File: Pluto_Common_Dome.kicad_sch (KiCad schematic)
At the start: 36 parts

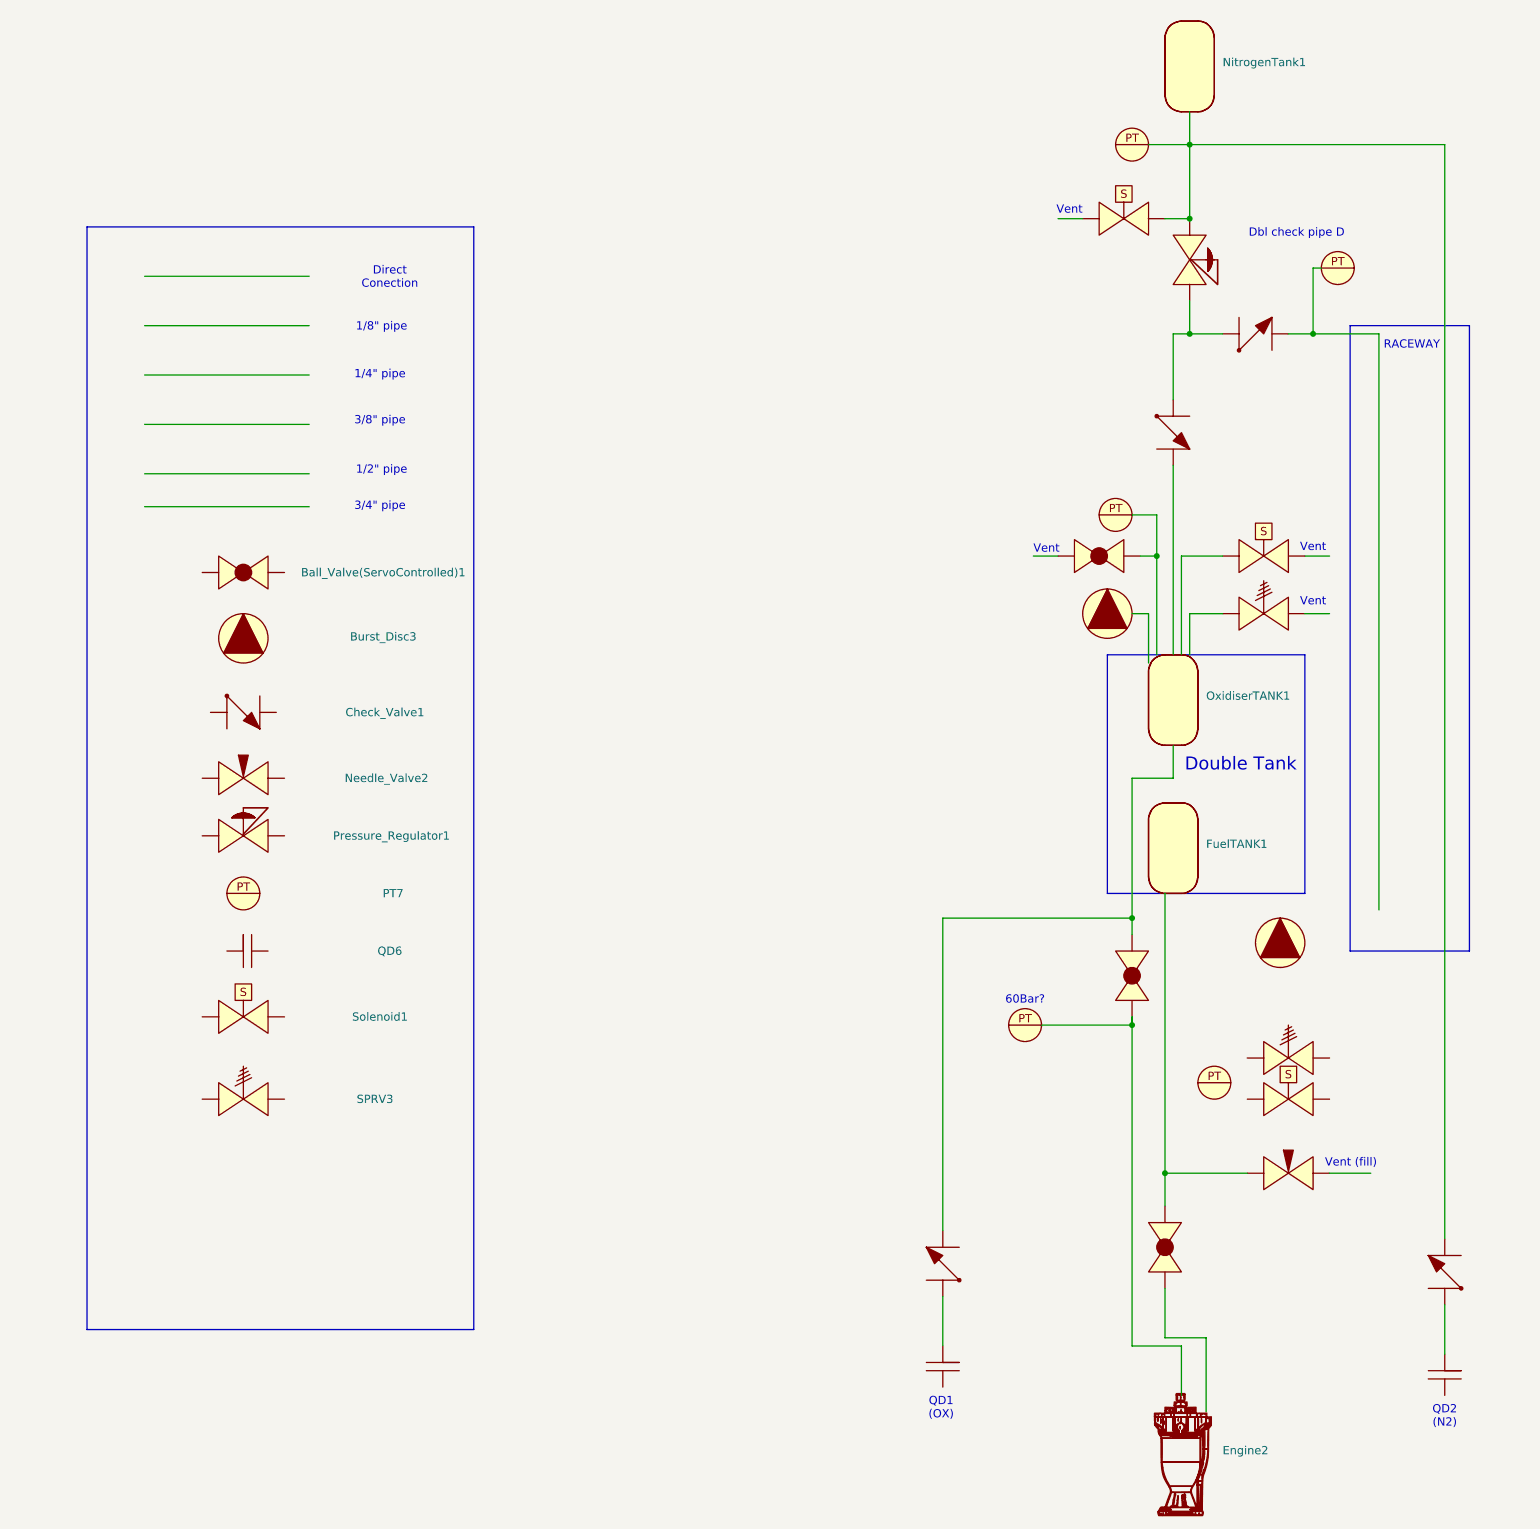
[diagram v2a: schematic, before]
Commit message: Updated Pluto P&ID
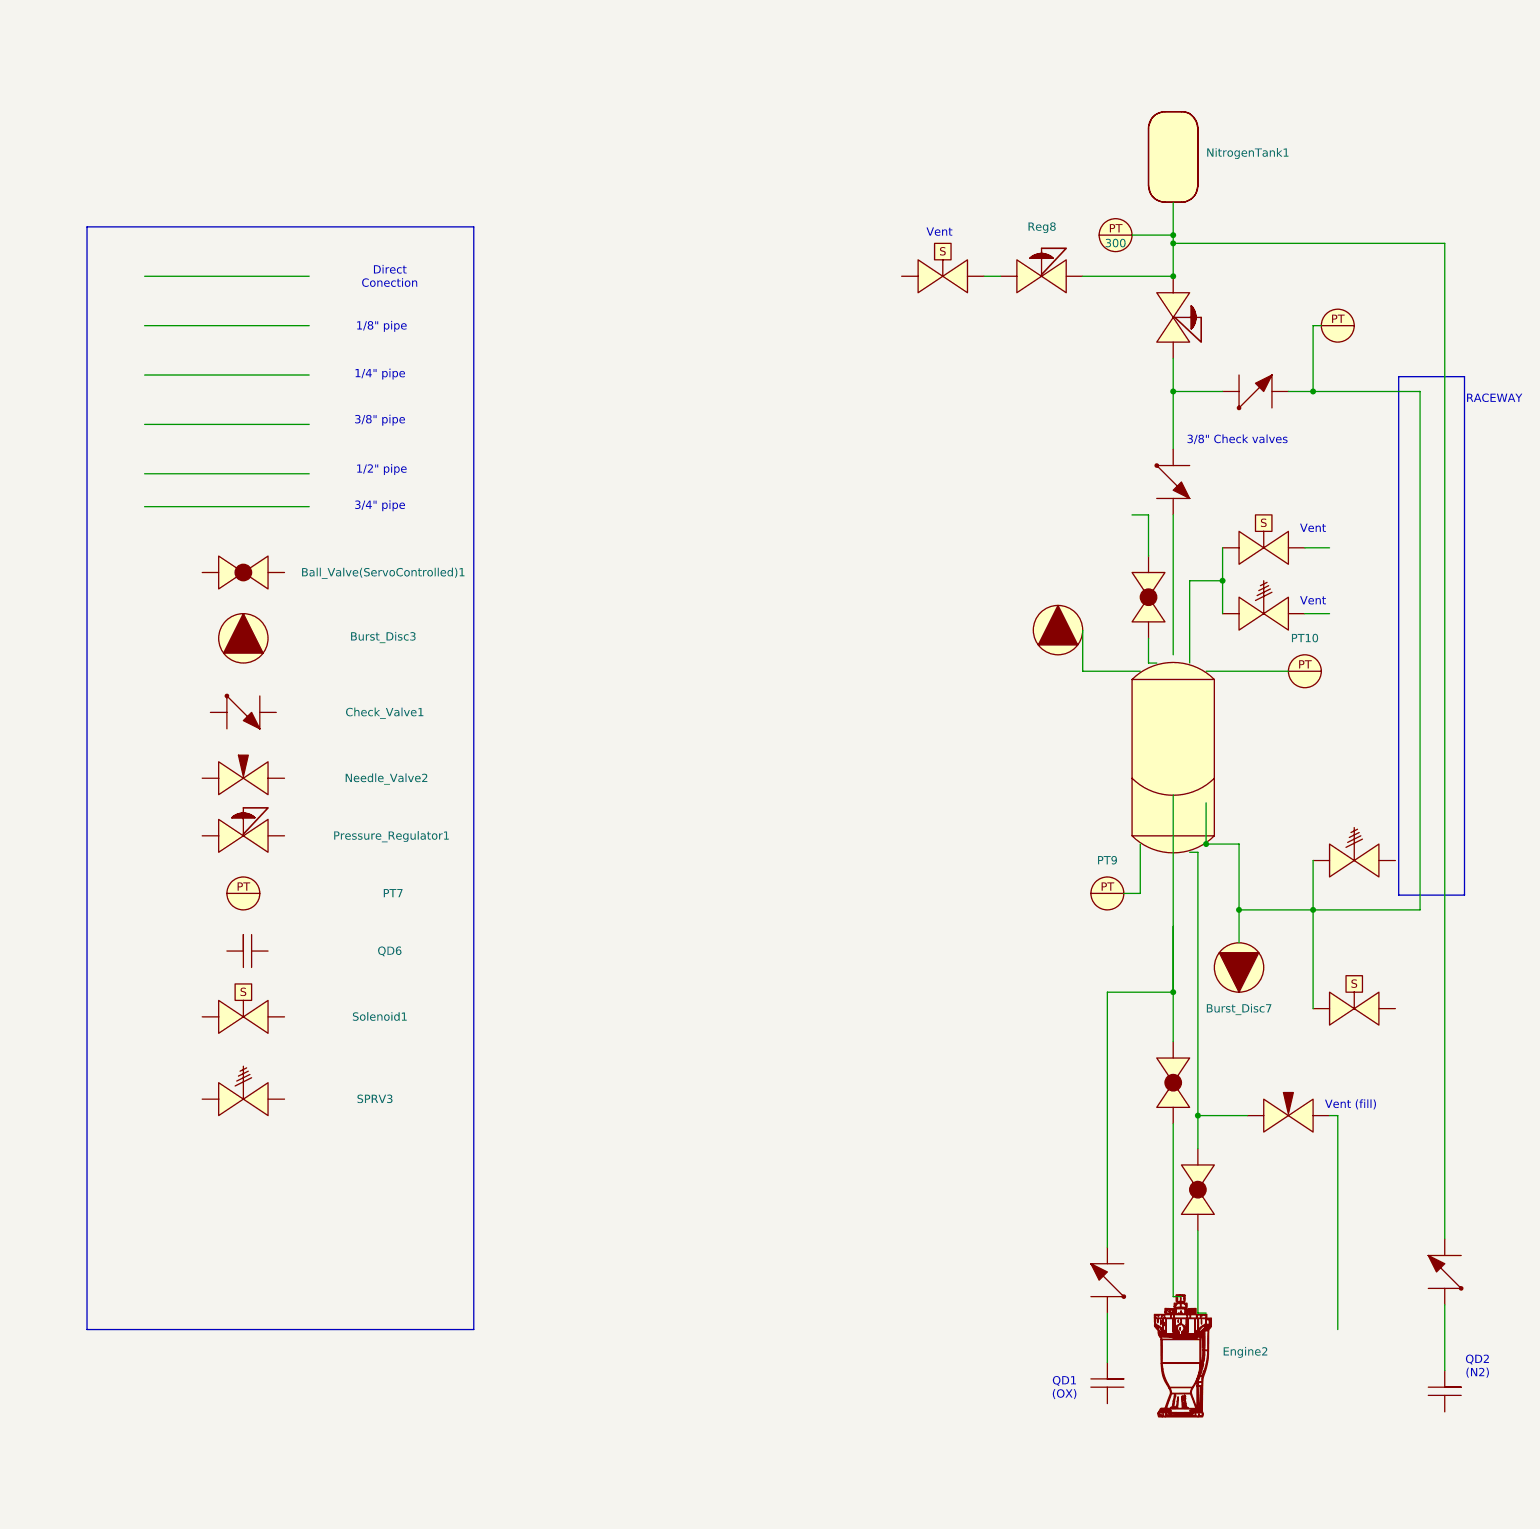
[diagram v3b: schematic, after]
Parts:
- removed Burst_Disc5: ~, symbol PID_symbols:Burst_Disc
- removed FuelTANK1, OxidiserTANK1: ~, symbol PID_symbols:Tank
- removed PT13: ~, symbol PID_symbols:Pressure_Transducer
- added Burst_Disc7: ~, symbol PID_symbols:Burst_Disc
- added CommonDomeTank1: ~, symbol PID_symbols:Common_Dome_Tank
- added Reg8: ~, symbol PID_symbols:Pressure_Regulator
- PT11: value ~ -> 300
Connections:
- net at Solenoid4.: now also Check_Valve4., PT14., SPRV5., Burst_Disc7., CommonDomeTank1.
- net at PT9.: now also CommonDomeTank1.
- net at Solenoid3.: now also SPRV4., CommonDomeTank1.
- net at Ball_Valve2.: now also Engine2.; no longer Check_Valve2.
- net at Needle_Valve3.: no longer Ball_Valve3.
- net at Check_Valve2.: now also QD8.; no longer QD7.
- net at Ball_Valve1.: now also CommonDomeTank1.
- net at PT10.: now also CommonDomeTank1.; no longer Ball_Valve1.
- net at Check_Valve5.: now also QD7.; no longer QD8.
- net at Burst_Disc4.: now also CommonDomeTank1.
- new net: Ball_Valve2., Check_Valve2., CommonDomeTank1.
- new net: Ball_Valve3., CommonDomeTank1., Needle_Valve3.
- new net: Check_Valve5., NitrogenTank1., PT11., Pressure_Regulator2., Reg8.
- new net: Reg8., Solenoid2.
- now unconnected: Engine2., NitrogenTank1., PT11., PT14., Solenoid2.
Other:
- note added: "3/8" Check valves"
- note removed: "60Bar?"
- note removed: "Dbl check pipe D"
- note removed: "Double Tank"
- moved on the sheet: Engine2, NitrogenTank1

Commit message: added universal key
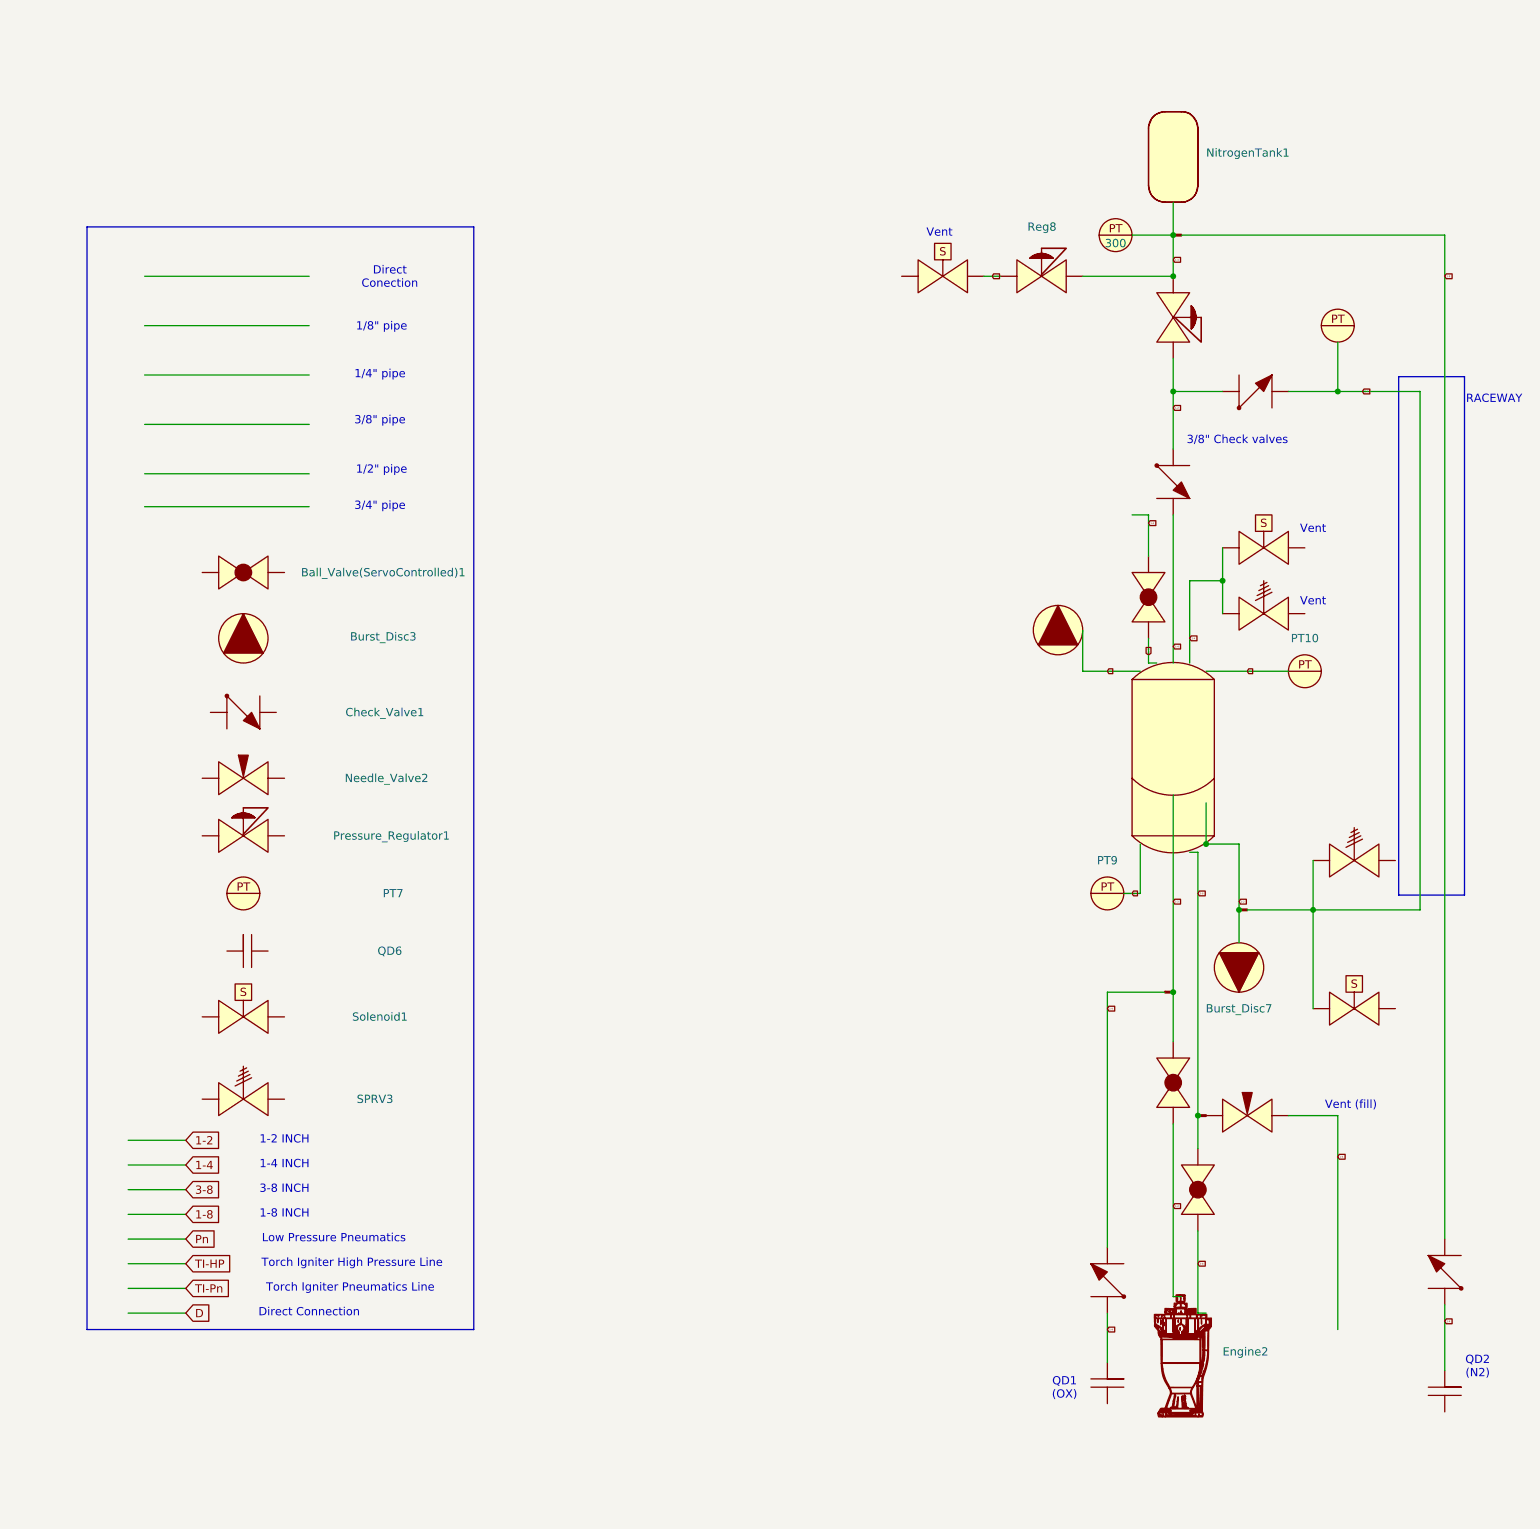
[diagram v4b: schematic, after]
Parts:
- added U2, U3, U4, U5: ~, symbol PID_symbols:stop
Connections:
- net 1-4: now reaches Solenoid4.
- net 1-4: now also Ball_Valve1., Check_Valve2., Check_Valve3., Check_Valve4., Check_Valve5., CommonDomeTank1., Needle_Valve3., NitrogenTank1., PT11., PT14., Pressure_Regulator2., QD7., QD8., Reg8., SPRV4., SPRV5., Solenoid2., Solenoid3., U2., U3., U5.
- net D: now reaches PT10.
- net D: now also Burst_Disc4., CommonDomeTank1., PT9.
- net 1-2: now reaches Ball_Valve2., Engine2.
- net 1-2: now also Burst_Disc7., Check_Valve3., Check_Valve4., CommonDomeTank1., Pressure_Regulator2., U2., U3.
- net 3-8: now reaches Ball_Valve3., Engine2.
- net 3-8: now also CommonDomeTank1., U4.
- net 1-8: now reaches Check_Valve5.
- net 1-8: now also U5.; no longer QD7.
- new net: Needle_Valve3., U4.
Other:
- note added: "1-2 INCH"
- note added: "1-4 INCH"
- note added: "1-8 INCH"
- note added: "3-8 INCH"
- note added: "Direct Connection"
- note added: "Low Pressure Pneumatics"
- note added: "Torch Igniter High Pressure Line"
- note added: "Torch Igniter Pneumatics Line"

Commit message: Small visual changes
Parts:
- added CommonDomeTank2: ~, symbol PID_symbols:Common_Dome_Tank
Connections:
- new net: Needle_Valve3., U4.
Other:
- note added: "Common Dome Tank (Oxidiser upper section, fuel lower section)"
- note added: "Pressure Transducer"
- note added: "Quick Disconnect"
- note added: "Safety Pressure Relief Valve"
- note removed: "1/2" pipe"
- note removed: "1/4" pipe"
- note removed: "1/8" pipe"
- note removed: "3/4" pipe"
- note removed: "3/8" pipe"
- note removed: "Direct Conection"
- moved on the sheet: Ball_Valve(ServoControlled)1, Burst_Disc3, Check_Valve1, Needle_Valve2, Pressure_Regulator1, Solenoid1

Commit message: Pluto pts
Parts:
- added PT15, PT37, PT38: ~, symbol PID_symbols:Pressure_Transducer
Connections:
- net 1-2: now also PT38.
- net 3-8: now also PT15.
- new net: Needle_Valve3., U4.
- new net: Engine2., PT37.

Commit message: sensibl4
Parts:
- added Engine3: ~, symbol PID_symbols:Engine
- added Tank200: Pressurant Tank, symbol PID_symbols:Tank
- Ball_Valve(ServoControlled)100: renamed from Ball_Valve(ServoControlled)1; value ~ -> Servo Controlled Ball Valve
- BurstDisc123: renamed from Burst_Disc3; value ~ -> Burst Disc
- Check_Valve112: renamed from Check_Valve1; value ~ -> Check Valve
- Pressure_Regulator123: renamed from Pressure_Regulator1; value ~ -> Pressure Regulator
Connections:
- net at PT37.: no longer Engine2.
- new net: Needle_Valve3., U4.
- new net: Engine2., PT37.
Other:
- note added: "Engine"
- note added: "Fuel Fill"
- note added: "Manual Valve"
- note added: "Solenoid Valve"
- note removed: "3/8" Check valves"
- note removed: "Vent"
- note removed: "Vent (fill)"
- title: Pluto Common Dome P&ID -> Pluto Propulsion P&ID

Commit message: ereg
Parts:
- removed Pressure_Regulator2: ~, symbol PID_symbols:Pressure_Regulator
- added BV11: ~, symbol PID_symbols:Ball_Valve
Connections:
- net 1-2: no longer Check_Valve3., Check_Valve4.
- net 1-4: now also BV11.
- net 3-8: now also Check_Valve3., Check_Valve4., BV11.
- net at PT37.: no longer Engine2.
- new net: Needle_Valve3., U4.
- new net: Engine2., PT37.
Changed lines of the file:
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@@
+	)
+	(junction
+		(at 144.78 55.88)
+		(diameter 0)
+		(color 0 0 0 0)
 	)
 	(junction
@@
 	)
 	(junction
-		(at 144.78 55.88)
-		(diameter 0)
-		(color 0 0 0 0)
-	)
-	(junction
 		(at 148.59 185.42)
 		(diameter 0)
@@
 	(wire
 		(pts
-			(xy 144.78 68.58) (xy 144.78 73.66)
-		)
-		(stroke
-			(width 0)
-			(type default)
-		)
-	)
-	(wire
-		(pts
 			(xy 140.97 115.57) (xy 142.24 115.57)
 		)
@@
 		(pts
 			(xy 138.43 92.71) (xy 140.97 92.71)
+		)
+		(stroke
+			(width 0)
+			(type default)
+		)
+	)
+	(wire
+		(pts
+			(xy 144.78 72.39) (xy 144.78 73.66)
 		)
 		(stroke
@@
 	(wire
 		(pts
+			(xy 144.78 59.69) (xy 144.78 55.88)
+		)
+		(stroke
+			(width 0)
+			(type default)
+		)
+	)
+	(wire
+		(pts
 			(xy 152.4 102.87) (xy 152.4 107.95)
 		)
@@
 		)
 	)
-	(global_label "1-2"
+	(global_label "3-8"
 		(shape input)
 		(at 144.78 76.2 0)
@@
 	)
 	(symbol
+		(lib_name "Ball_Valve_4")
+		(lib_id "PID_symbols:Ball_Valve")
+		(at 144.78 69.85 90)
+		(unit 1)
+		(exclude_from_sim no)
+		(in_bom yes)
+		(on_board yes)
+		(dnp no)
+		(fields_autoplaced yes)
+		(property "Reference" "BV11"
+			(at 148.59 65.4049 90)
+			(effects
+				(font
+					(size 1.27 1.27)
+				)
+				(justify right)
+				(hide yes)
+			)
+		)
+		(property "Value" "~"
+			(at 148.59 67.31 90)
+			(effects
+				(font
+					(size 1.27 1.27)
+				)
+				(justify right)
+			)
+		)
+		(property "Footprint" ""
+			(at 144.78 69.85 0)
+			(effects
+				(font
+					(size 1.27 1.27)
+				)
+				(hide yes)
+			)
+		)
+		(property "Datasheet" ""
+			(at 144.78 69.85 0)
+			(effects
+				(font
+					(size 1.27 1.27)
+				)
+				(hide yes)
+			)
+		)
+		(property "Description" ""
+			(at 144.78 69.85 0)
+			(effects
+				(font
+					(size 1.27 1.27)
+				)
+				(hide yes)
+			)
+		)
+		(pin ""
+		)
+		(pin ""
+		)
+		(instances
+			(project ""
+				(path "/045f1f05-3134-4b6d-91b6-463031104f1e/561f91da-59dd-4c39-b4eb-a17d4e7f8654"
+					(reference "BV11")
+					(unit 1)
+				)
+			)
+		)
+	)
+	(symbol
 		(lib_id "PID_symbols:SPRV")
 		(at 25.4 176.53 0)
@@
 					(unit 1)
 				)
-			)
-		)
-	)
-	(symbol
-		(lib_name "Pressure_Regulator_2")
-		(lib_id "PID_symbols:Pressure_Regulator")
-		(at 144.78 58.42 270)
-		(unit 1)
-		(exclude_from_sim no)
-		(in_bom yes)
-		(on_board yes)
-		(dnp no)
-		(fields_autoplaced yes)
-		(property "Reference" "Pressure_Regulator2"
-			(at 152.4 62.2925 0)
-			(effects
-				(font
-					(size 1.27 1.27)
-				)
-				(hide yes)
-			)
-		)
-		(property "Value" "~"
-			(at 149.86 62.2925 90)
-			(effects
-				(font
-					(size 1.27 1.27)
-				)
-				(justify left)
-			)
-		)
-		(property "Footprint" ""
-			(at 144.78 58.42 0)
-			(effects
-				(font
-					(size 1.27 1.27)
-				)
-				(hide yes)
-			)
-		)
-		(property "Datasheet" ""
-			(at 144.78 58.42 0)
-			(effects
-				(font
-					(size 1.27 1.27)
-				)
-				(hide yes)
-			)
-		)
-		(property "Description" "Pressure Regulator"
-			(at 144.78 58.42 0)
-			(effects
-				(font
-					(size 1.27 1.27)
-				)
-				(hide yes)
-			)
-		)
-		(pin ""
-		)
-		(pin ""
-		)
-		(instances
-			(project "P_IDs"
-				(path "/045f1f05-3134-4b6d-91b6-463031104f1e/561f91da-59dd-4c39-b4eb-a17d4e7f8654"
-					(reference "Pressure_Regulator2")
-					(unit 1)
-				)
